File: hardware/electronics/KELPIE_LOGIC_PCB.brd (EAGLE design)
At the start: 101.6 x 57.1 mm, 55 parts, among them J1 PJ-002A, J3 30_PIN_CONNECTOR_MALEFLEX_CON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, J5 SWITCHCRAFT_PHONEJACK, J6 SWD_CONNECTOR, T2 MCP1825S, U4 SGTL5000_32QFN, U5 23LC1024

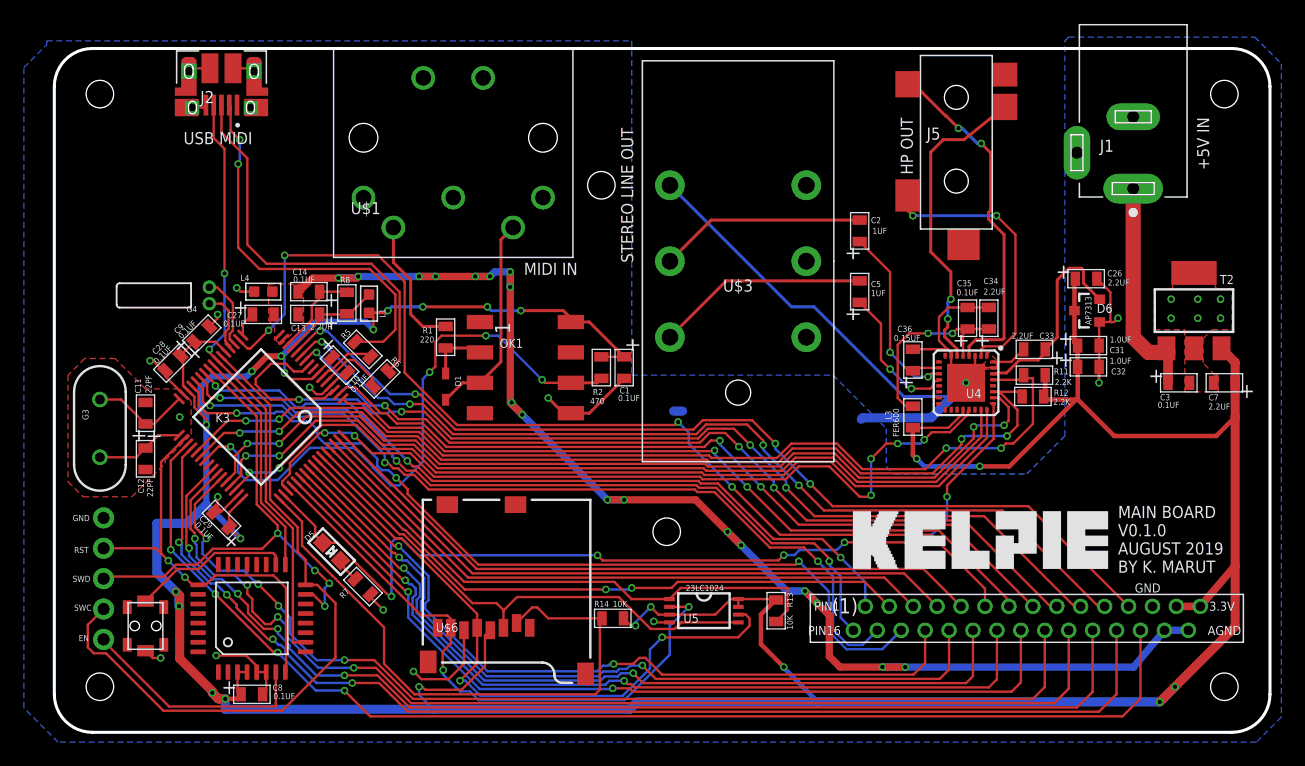
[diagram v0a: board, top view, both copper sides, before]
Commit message: board rev 2 done, sent to seeed for manufacture
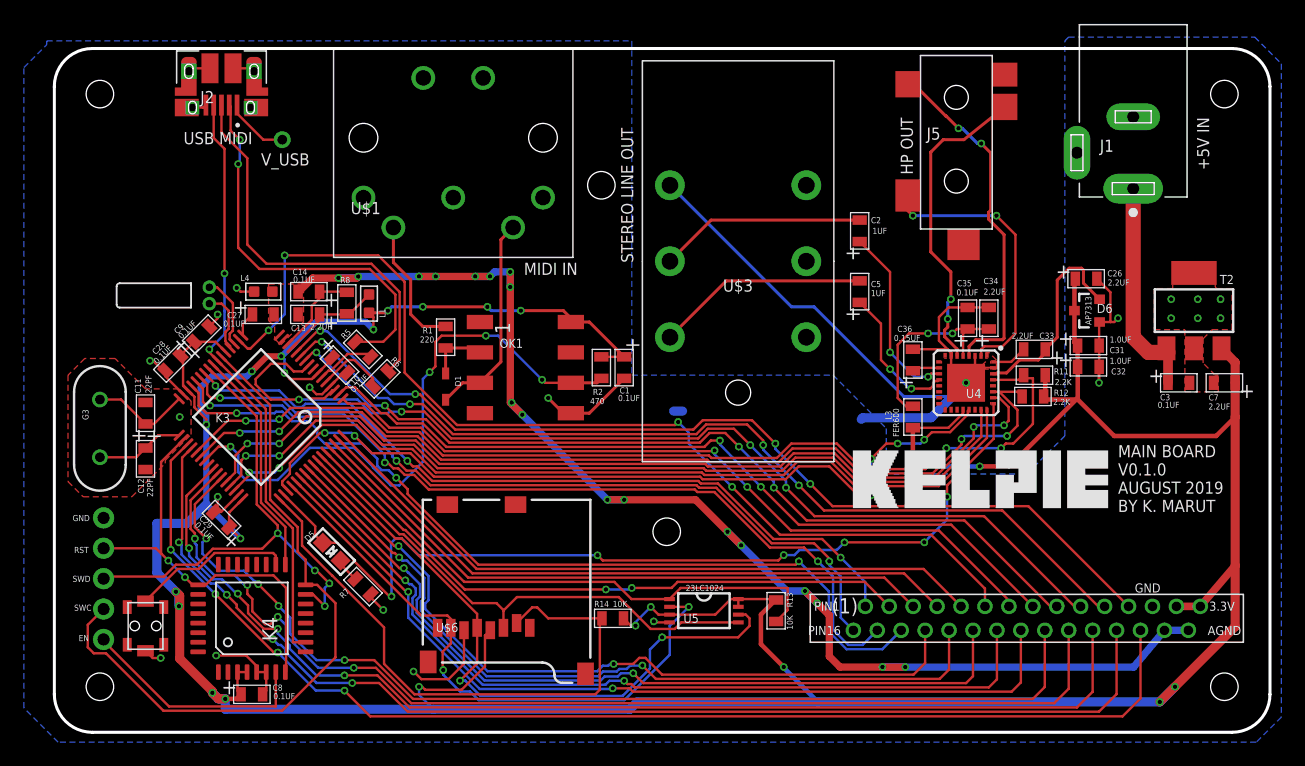
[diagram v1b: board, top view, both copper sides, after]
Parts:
- added U$2: TEST_POINT, sirin-clone-library:TEST_POINT
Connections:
- net VUSB_IN: now also U$2.P$1
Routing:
- net VUSB_IN: track 0.00 -> 5.41 mm
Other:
- board text added: "V_USB"

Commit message: working on bom
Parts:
- C10, C13, C14, C26, C27, C28, C29, C3, C33, C34, C35, C36, C7, C8, C9: device moon-germs-v1_main:C_0805 -> sirin-clone-library:C_0805
- C31, C32: value 1.0UF -> 1UF; device moon-germs-v1_main:C_0805 -> sirin-clone-library:C_0805
- J3: device sirin-clone-library:SLW30S -> sirin-clone-library:SLW30S_TOP
- R11, R12, R13, R14: device moon-germs-v1_main:0805 -> sirin-clone-library:0805
- S2: device moon-germs-v1_main:SWITCH_PTS820 -> sirin-clone-library:SWITCH_PTS820

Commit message: update readme
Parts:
- C11, C12: device moon-germs-v1_main:C_0805 -> sirin-clone-library:C_0805
- D5: device moon-germs-v1_main:CHIPLED_0805 -> sirin-clone-library:CHIPLED_0805
- D6: device moon-germs-v1_main:SOT23-3 -> sirin-clone-library:SOT23-3
- L3, R5, R6, R7, R8: device moon-germs-v1_main:0805 -> sirin-clone-library:0805
- U$6: device moon-germs-v1_main:MICRO-SD-SOCKET -> sirin-clone-library:MICRO-SD-SOCKET
- U4: device moon-germs-v1_main:QFN-32-5MM -> sirin-clone-library:QFN-32-5MM
- U5: device moon-germs-v1_main:TSSOP8 -> sirin-clone-library:TSSOP8

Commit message: hotfix, reexported BOM in BOM folder
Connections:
- net N$20 renamed 1.8V
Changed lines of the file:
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@@
 <drawing>
 <settings>
-<setting alwaysvectorfont="yes"/>
+<setting alwaysvectorfont="no"/>
 <setting verticaltext="up"/>
 </settings>
@@
 </element>
 <element name="C7" library="sirin-clone-library" library_urn="urn:adsk.eagle:library:9336050" package="C_0805" package3d_urn="urn:adsk.eagle:package:8442351/2" value="2.2UF" x="97.79" y="29.21" smashed="yes" rot="R180">
-<attribute name="MPN" value="CL21B105KAFNNNE" x="97.79" y="29.21" size="1.778" layer="27" rot="R180" display="off"/>
+<attribute name="MPN" value="CL21B225KAFNFNE" x="97.79" y="29.21" size="1.778" layer="27" rot="R180" display="off"/>
 <attribute name="NAME" x="96.4692" y="27.7368" size="0.508" layer="21"/>
 <attribute name="VALUE" x="96.4565" y="26.9748" size="0.508" layer="21"/>
@@
 </element>
 <element name="C13" library="sirin-clone-library" library_urn="urn:adsk.eagle:library:9336050" package="C_0805" package3d_urn="urn:adsk.eagle:package:8442351/2" value="2.2UF" x="21.272" y="34.925" smashed="yes" rot="R180">
-<attribute name="MPN" value="CL21B105KAFNNNE" x="21.272" y="34.925" size="1.778" layer="27" rot="R180" display="off"/>
+<attribute name="MPN" value="CL21B225KAFNFNE" x="21.272" y="34.925" size="1.778" layer="27" rot="R180" display="off"/>
 <attribute name="NAME" x="21.018" y="34.036" size="0.508" layer="21" rot="R180"/>
 <attribute name="VALUE" x="23.177" y="34.163" size="0.508" layer="21" rot="R180"/>
@@
 </element>
 <element name="C26" library="sirin-clone-library" library_urn="urn:adsk.eagle:library:9336050" package="C_0805" package3d_urn="urn:adsk.eagle:package:8442351/2" value="2.2UF" x="86.233" y="37.91" smashed="yes">
-<attribute name="MPN" value="CL21B105KAFNNNE" x="86.233" y="37.91" size="1.778" layer="27" display="off"/>
+<attribute name="MPN" value="CL21B225KAFNFNE" x="86.233" y="37.91" size="1.778" layer="27" display="off"/>
 <attribute name="NAME" x="88.011" y="38.1005" size="0.508" layer="21"/>
 <attribute name="VALUE" x="89.8525" y="37.8465" size="0.508" layer="21" rot="R180"/>
@@
 </element>
 <element name="C33" library="sirin-clone-library" library_urn="urn:adsk.eagle:library:9336050" package="C_0805" package3d_urn="urn:adsk.eagle:package:8442351/2" value="2.2UF" x="81.915" y="32.004" smashed="yes" rot="R180">
-<attribute name="MPN" value="CL21B105KAFNNNE" x="81.915" y="32.004" size="1.778" layer="27" rot="R180" display="off"/>
+<attribute name="MPN" value="CL21B225KAFNFNE" x="81.915" y="32.004" size="1.778" layer="27" rot="R180" display="off"/>
 <attribute name="NAME" x="83.566" y="33.401" size="0.508" layer="21" rot="R180"/>
 <attribute name="VALUE" x="80.01" y="32.893" size="0.508" layer="21"/>
 </element>
 <element name="C34" library="sirin-clone-library" library_urn="urn:adsk.eagle:library:9336050" package="C_0805" package3d_urn="urn:adsk.eagle:package:8442351/2" value="2.2UF" x="78.105" y="34.608" smashed="yes" rot="R90">
-<attribute name="MPN" value="CL21B105KAFNNNE" x="78.105" y="34.608" size="1.778" layer="27" rot="R90" display="off"/>
+<attribute name="MPN" value="CL21B225KAFNFNE" x="78.105" y="34.608" size="1.778" layer="27" rot="R90" display="off"/>
 <attribute name="NAME" x="77.6605" y="37.4655" size="0.508" layer="21"/>
 <attribute name="VALUE" x="77.6605" y="36.5765" size="0.508" layer="21"/>
@@
 </element>
 <element name="D6" library="sirin-clone-library" library_urn="urn:adsk.eagle:library:9336050" package="SOT23-3" package3d_urn="urn:adsk.eagle:package:8442353/2" value="AP7313" x="86.36" y="35.242" smashed="yes" rot="R90">
-<attribute name="MPN" value="AP7313-33SRG-7" x="86.36" y="35.242" size="1.778" layer="27" rot="R90" display="off"/>
+<attribute name="MPN" value="AP7313-18SRG-7" x="86.36" y="35.242" size="1.778" layer="27" rot="R90" display="off"/>
 <attribute name="VALUE" x="86.1695" y="36.4485" size="0.508" layer="21" rot="R270"/>
 </element>
@@
 <wire x1="80.3275" y1="41.5925" x2="78.74" y2="43.18" width="0.2032" layer="1"/>
 </signal>
-<signal name="N$20">
+<signal name="1.8V">
 <contactref element="C33" pad="+"/>
 <contactref element="D6" pad="OUT"/>
